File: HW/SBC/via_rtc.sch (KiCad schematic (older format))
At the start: 5 parts, among them J2 CONN_02X07, J3 CONN_02X07, U6 WD65C22, U7 DS1511Y+

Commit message: Updates to pcb and monitor.
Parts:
- J2, J3: footprint Pin_Headers:Pin_Header_Straight_2x07_Pitch2.54mm -> Connect:IDC_Header_Straight_14pins
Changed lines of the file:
@@
 F 0 "J2" H 1550 2825 50  0000 C CNN
 F 1 "CONN_02X07" V 1550 2425 50  0000 C CNN
-F 2 "Pin_Headers:Pin_Header_Straight_2x07_Pitch2.54mm" H 1550 1225 50  0001 C CNN
+F 2 "Connect:IDC_Header_Straight_14pins" H 1550 1225 50  0001 C CNN
 F 3 "" H 1550 1225 50  0001 C CNN
 	1    1550 2425
@@
 F 0 "J3" H 1550 4350 50  0000 C CNN
 F 1 "CONN_02X07" V 1550 3950 50  0000 C CNN
-F 2 "Pin_Headers:Pin_Header_Straight_2x07_Pitch2.54mm" H 1550 2750 50  0001 C CNN
+F 2 "Connect:IDC_Header_Straight_14pins" H 1550 2750 50  0001 C CNN
 F 3 "" H 1550 2750 50  0001 C CNN
 	1    1550 3950
@@
 $EndComp
 $Comp
-L VCC #PWR012
+L VCC #PWR013
 U 1 1 58D69383
 P 1125 4350
-F 0 "#PWR012" H 1125 4200 50  0001 C CNN
+F 0 "#PWR013" H 1125 4200 50  0001 C CNN
 F 1 "VCC" H 1125 4500 50  0000 C CNN
 F 2 "" H 1125 4350 50  0001 C CNN
@@
 $EndComp
 $Comp
-L GND #PWR013
+L GND #PWR014
 U 1 1 58D6939F
 P 1125 3450
-F 0 "#PWR013" H 1125 3200 50  0001 C CNN
+F 0 "#PWR014" H 1125 3200 50  0001 C CNN
 F 1 "GND" H 1125 3300 50  0000 C CNN
 F 2 "" H 1125 3450 50  0001 C CNN
@@
 $EndComp
 $Comp
-L GND #PWR014
+L GND #PWR015
 U 1 1 58D6973D
 P 1125 1950
-F 0 "#PWR014" H 1125 1700 50  0001 C CNN
+F 0 "#PWR015" H 1125 1700 50  0001 C CNN
 F 1 "GND" H 1125 1800 50  0000 C CNN
 F 2 "" H 1125 1950 50  0001 C CNN
@@
 $EndComp
 $Comp
-L VCC #PWR015
+L VCC #PWR016
 U 1 1 58D69759
 P 1125 2825
-F 0 "#PWR015" H 1125 2675 50  0001 C CNN
+F 0 "#PWR016" H 1125 2675 50  0001 C CNN
 F 1 "VCC" H 1125 2975 50  0000 C CNN
 F 2 "" H 1125 2825 50  0001 C CNN
@@
 $EndComp
 $Comp
-L VCC #PWR016
+L VCC #PWR017
 U 1 1 58D6982A
 P 4275 3550
-F 0 "#PWR016" H 4275 3400 50  0001 C CNN
+F 0 "#PWR017" H 4275 3400 50  0001 C CNN
 F 1 "VCC" H 4275 3700 50  0000 C CNN
 F 2 "" H 4275 3550 50  0001 C CNN
@@
 ~RES
 $Comp
-L GND #PWR017
+L GND #PWR018
 U 1 1 58D6B152
 P 7825 3725
-F 0 "#PWR017" H 7825 3475 50  0001 C CNN
+F 0 "#PWR018" H 7825 3475 50  0001 C CNN
 F 1 "GND" H 7825 3575 50  0000 C CNN
 F 2 "" H 7825 3725 50  0001 C CNN
@@
 $EndComp
 $Comp
-L VCC #PWR018
+L VCC #PWR019
 U 1 1 58D6B2C3
 P 7900 1850
-F 0 "#PWR018" H 7900 1700 50  0001 C CNN
+F 0 "#PWR019" H 7900 1700 50  0001 C CNN
 F 1 "VCC" H 7900 2000 50  0000 C CNN
 F 2 "" H 7900 1850 50  0001 C CNN
@@
 The intention is to use a WDC65C22\nso a diod has been added.
 $Comp
-L VCC #PWR019
+L VCC #PWR020
 U 1 1 58D8610D
 P 3400 1550
-F 0 "#PWR019" H 3400 1400 50  0001 C CNN
+F 0 "#PWR020" H 3400 1400 50  0001 C CNN
 F 1 "VCC" H 3400 1700 50  0000 C CNN
 F 2 "" H 3400 1550 50  0001 C CNN
@@
 	8450 2975 8775 2975
 $Comp
-L GND #PWR020
+L GND #PWR021
 U 1 1 58D875DB
 P 3400 4825
-F 0 "#PWR020" H 3400 4575 50  0001 C CNN
+F 0 "#PWR021" H 3400 4575 50  0001 C CNN
 F 1 "GND" H 3400 4675 50  0000 C CNN
 F 2 "" H 3400 4825 50  0001 C CNN

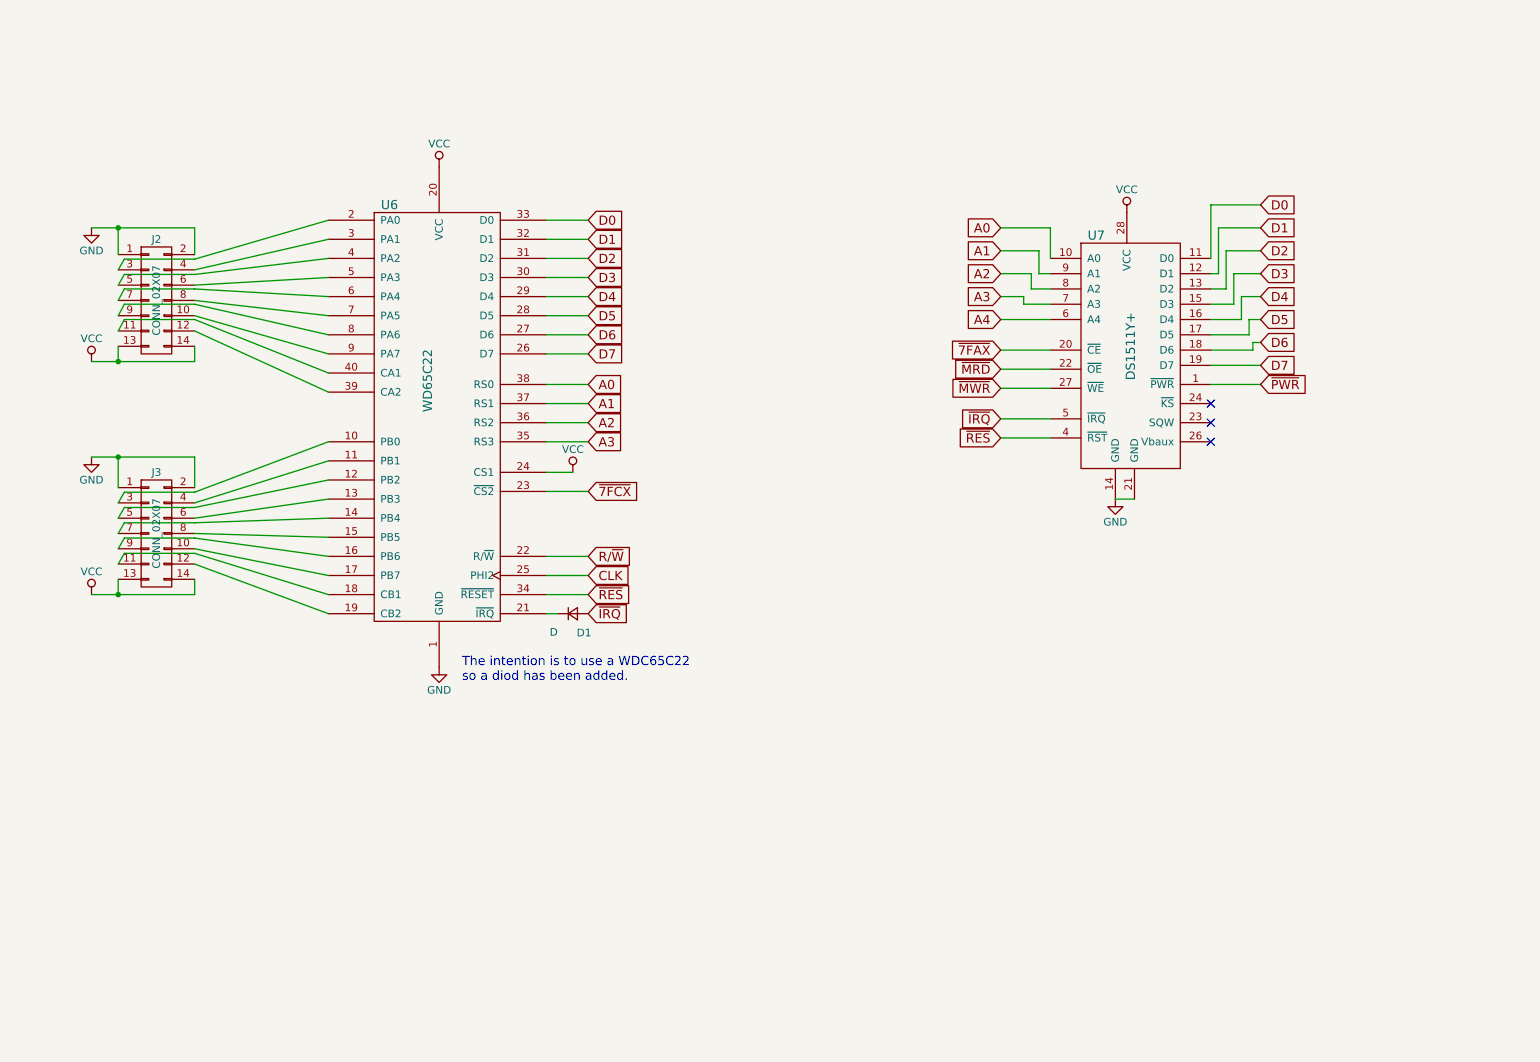
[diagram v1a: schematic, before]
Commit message: Schema changes to SBC
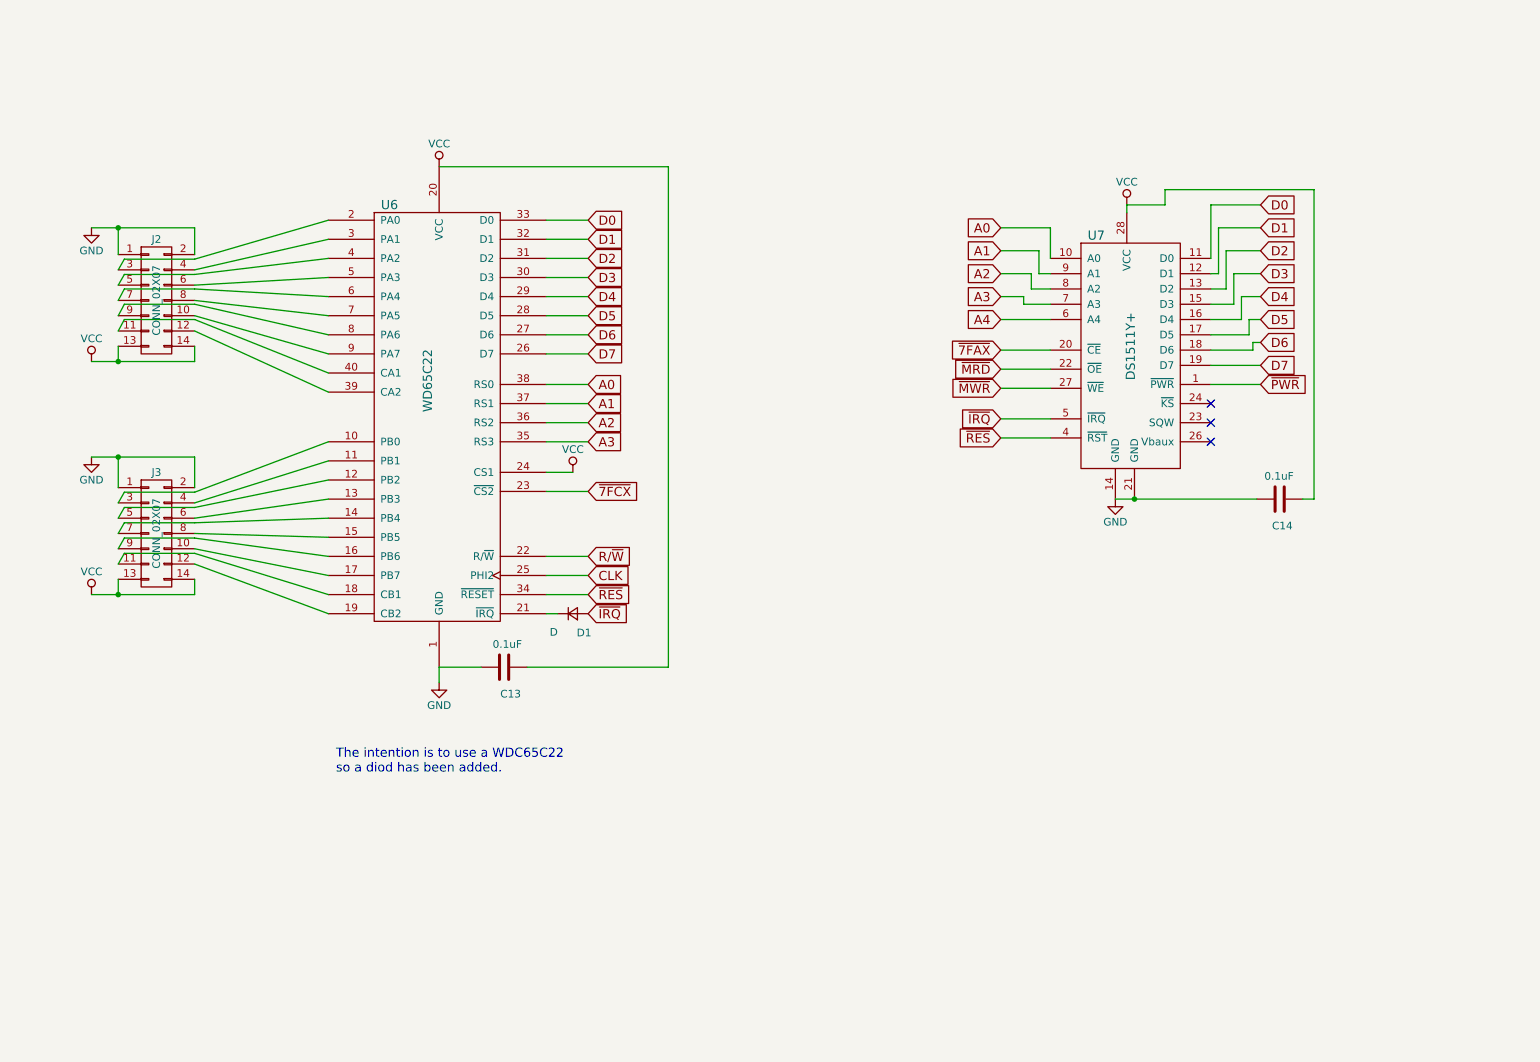
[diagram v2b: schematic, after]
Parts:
- added C13, C14: 0.1uF, Capacitors_ThroughHole:C_Disc_D3.8mm_W2.6mm_P2.50mm, symbol C
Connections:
- net GND: now also C13.2, C14.2
- net VCC: now also C13.1, C14.1
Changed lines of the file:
@@
 L VCC #PWR019
 U 1 1 58D6B2C3
-P 7900 1850
-F 0 "#PWR019" H 7900 1700 50  0001 C CNN
-F 1 "VCC" H 7900 2000 50  0000 C CNN
-F 2 "" H 7900 1850 50  0001 C CNN
-F 3 "" H 7900 1850 50  0001 C CNN
-	1    7900 1850
+P 7900 1800
+F 0 "#PWR019" H 7900 1650 50  0001 C CNN
+F 1 "VCC" H 7900 1950 50  0000 C CNN
+F 2 "" H 7900 1800 50  0001 C CNN
+F 3 "" H 7900 1800 50  0001 C CNN
+	1    7900 1800
 	1    0    0    -1
 $EndComp
@@
 Text GLabel 8775 2975 2    60   Input ~ 0
 ~PWR
-Text Notes 3550 4925 0    60   ~ 0
+Text Notes 2725 5525 0    60   ~ 0
 The intention is to use a WDC65C22\nso a diod has been added.
 $Comp
@@
 	1    0    0    -1
 $EndComp
+$Comp
+L GND #PWR021
+U 1 1 58D875DB
+P 3400 4925
+F 0 "#PWR021" H 3400 4675 50  0001 C CNN
+F 1 "GND" H 3400 4775 50  0000 C CNN
+F 2 "" H 3400 4925 50  0001 C CNN
+F 3 "" H 3400 4925 50  0001 C CNN
+	1    3400 4925
+	1    0    0    -1
+$EndComp
+$Comp
+L C C13
+U 1 1 5907389E
+P 3825 4825
+F 0 "C13" V 4000 4800 50  0000 L CNN
+F 1 "0.1uF" V 3675 4750 50  0000 L CNN
+F 2 "Capacitors_ThroughHole:C_Disc_D3.8mm_W2.6mm_P2.50mm" H 3863 4675 50  0001 C CNN
+F 3 "" H 3825 4825 50  0001 C CNN
+	1    3825 4825
+	0    1    1    0
+$EndComp
 Wire Wire Line
 	7400 2550 7075 2550
@@
 	8450 1800 8775 1800
 Wire Wire Line
-	7950 3725 7825 3725
+	7825 3725 8750 3725
 Wire Wire Line
 	8450 2975 8775 2975
+Wire Wire Line
+	3400 4825 3400 4925
+Wire Wire Line
+	3675 4825 3400 4825
+Wire Wire Line
+	3975 4825 4900 4825
+Wire Wire Line
+	4900 4825 4900 1550
+Wire Wire Line
+	4900 1550 3400 1550
 $Comp
-L GND #PWR021
-U 1 1 58D875DB
-P 3400 4825
-F 0 "#PWR021" H 3400 4575 50  0001 C CNN
-F 1 "GND" H 3400 4675 50  0000 C CNN
-F 2 "" H 3400 4825 50  0001 C CNN
-F 3 "" H 3400 4825 50  0001 C CNN
-	1    3400 4825
-	1    0    0    -1
-$EndComp
+L C C14
+U 1 1 59074B76
+P 8900 3725
+F 0 "C14" V 9075 3675 50  0000 L CNN
+F 1 "0.1uF" V 8750 3625 50  0000 L CNN
+F 2 "Capacitors_ThroughHole:C_Disc_D3.8mm_W2.6mm_P2.50mm" H 8938 3575 50  0001 C CNN
+F 3 "" H 8900 3725 50  0001 C CNN
+	1    8900 3725
+	0    1    1    0
+$EndComp
+Connection ~ 7950 3725
+Wire Wire Line
+	7900 1850 7900 1800
+Wire Wire Line
+	9050 3725 9125 3725
+Wire Wire Line
+	9125 3725 9125 1700
+Wire Wire Line
+	9125 1700 8150 1700
+Wire Wire Line
+	8150 1700 8150 1800
+Wire Wire Line
+	8150 1800 7900 1800
 $EndSCHEMATC

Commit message: New board layout. WIP
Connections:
- net GND: no longer C13.2, C14.2, U6.1 (GND), U7.14 (GND), U7.21 (GND)
- net VCC: no longer C13.1, C14.1, U6.20 (VCC), U7.28 (VCC)
- new net: C13.2, U6.1 (GND)
- new net: C13.1, U6.20 (VCC)
- new net: C14.2, U7.14 (GND), U7.21 (GND)
- new net: C14.1, U7.28 (VCC)
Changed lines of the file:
@@
 Text GLabel 7075 3325 0    60   Input ~ 0
 ~RES
-$Comp
-L GND #PWR018
-U 1 1 58D6B152
-P 7825 3725
-F 0 "#PWR018" H 7825 3475 50  0001 C CNN
-F 1 "GND" H 7825 3575 50  0000 C CNN
-F 2 "" H 7825 3725 50  0001 C CNN
-F 3 "" H 7825 3725 50  0001 C CNN
-	1    7825 3725
-	1    0    0    -1
-$EndComp
-$Comp
-L VCC #PWR019
-U 1 1 58D6B2C3
-P 7900 1800
-F 0 "#PWR019" H 7900 1650 50  0001 C CNN
-F 1 "VCC" H 7900 1950 50  0000 C CNN
-F 2 "" H 7900 1800 50  0001 C CNN
-F 3 "" H 7900 1800 50  0001 C CNN
-	1    7900 1800
-	1    0    0    -1
-$EndComp
 NoConn ~ 8450 3100
 NoConn ~ 8450 3225
@@
 Text Notes 2725 5525 0    60   ~ 0
 The intention is to use a WDC65C22\nso a diod has been added.
-$Comp
-L VCC #PWR020
-U 1 1 58D8610D
-P 3400 1550
-F 0 "#PWR020" H 3400 1400 50  0001 C CNN
-F 1 "VCC" H 3400 1700 50  0000 C CNN
-F 2 "" H 3400 1550 50  0001 C CNN
-F 3 "" H 3400 1550 50  0001 C CNN
-	1    3400 1550
-	1    0    0    -1
-$EndComp
-$Comp
-L GND #PWR021
-U 1 1 58D875DB
-P 3400 4925
-F 0 "#PWR021" H 3400 4675 50  0001 C CNN
-F 1 "GND" H 3400 4775 50  0000 C CNN
-F 2 "" H 3400 4925 50  0001 C CNN
-F 3 "" H 3400 4925 50  0001 C CNN
-	1    3400 4925
-	1    0    0    -1
-$EndComp
 $Comp
 L C C13
@@
 	8450 2975 8775 2975
 Wire Wire Line
-	3400 4825 3400 4925
-Wire Wire Line
 	3675 4825 3400 4825
 Wire Wire Line
@@
 Wire Wire Line
 	4900 4825 4900 1550
-Wire Wire Line
-	4900 1550 3400 1550
 $Comp
 L C C14
@@
 Wire Wire Line
 	8150 1800 7900 1800
+Wire Wire Line
+	4900 1550 3400 1550
 $EndSCHEMATC

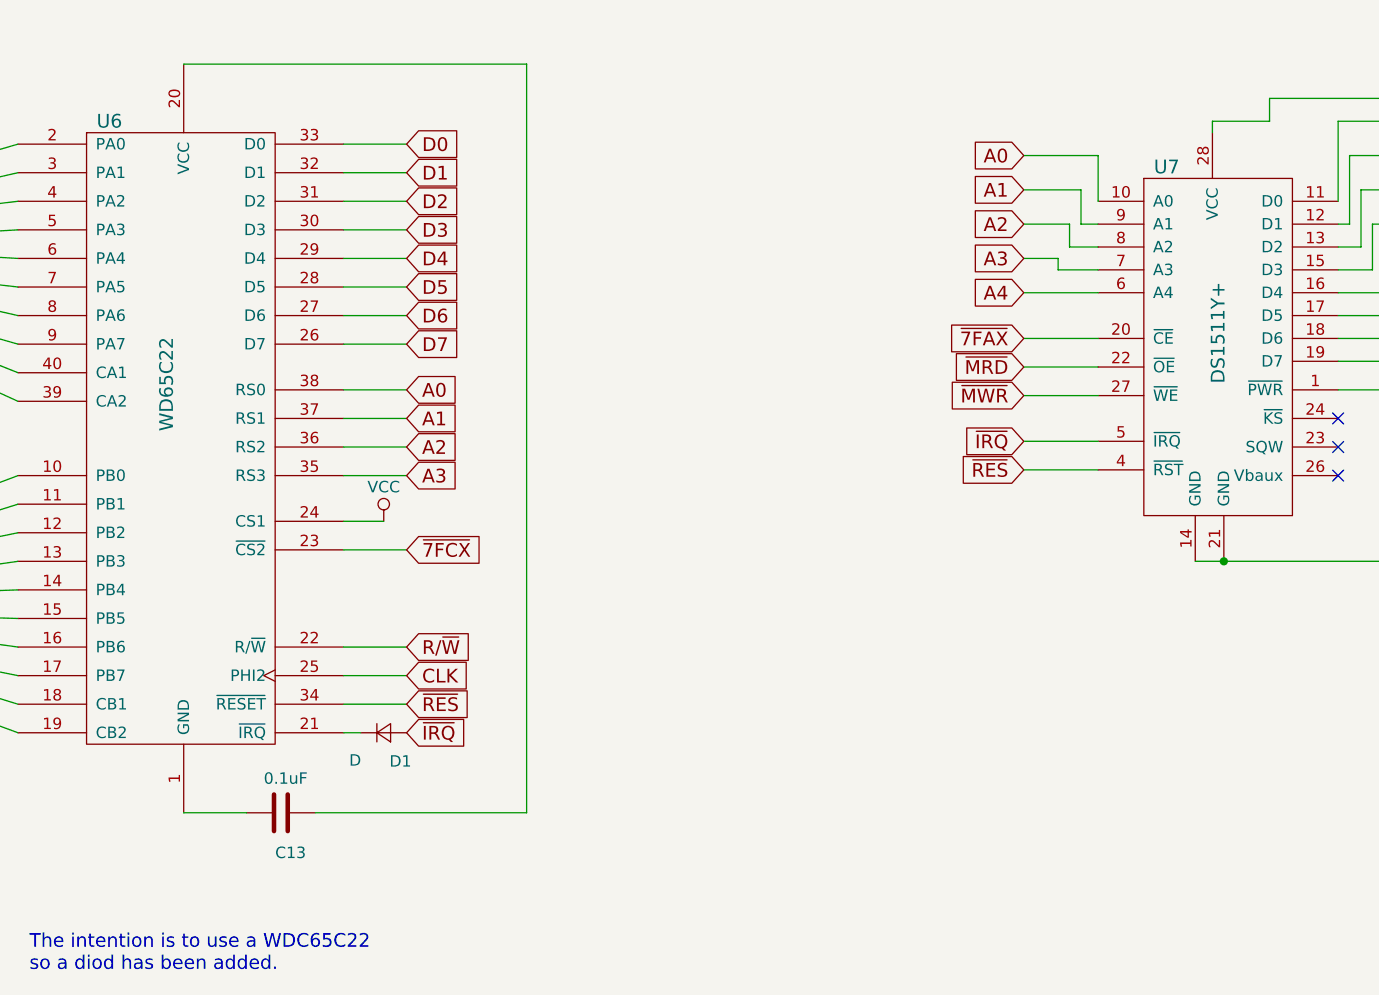
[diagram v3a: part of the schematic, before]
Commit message: New SBC PCB. Started to split pluto_kernel.asm into bios, monitor and miniassembler/disassembler. Various other updates.
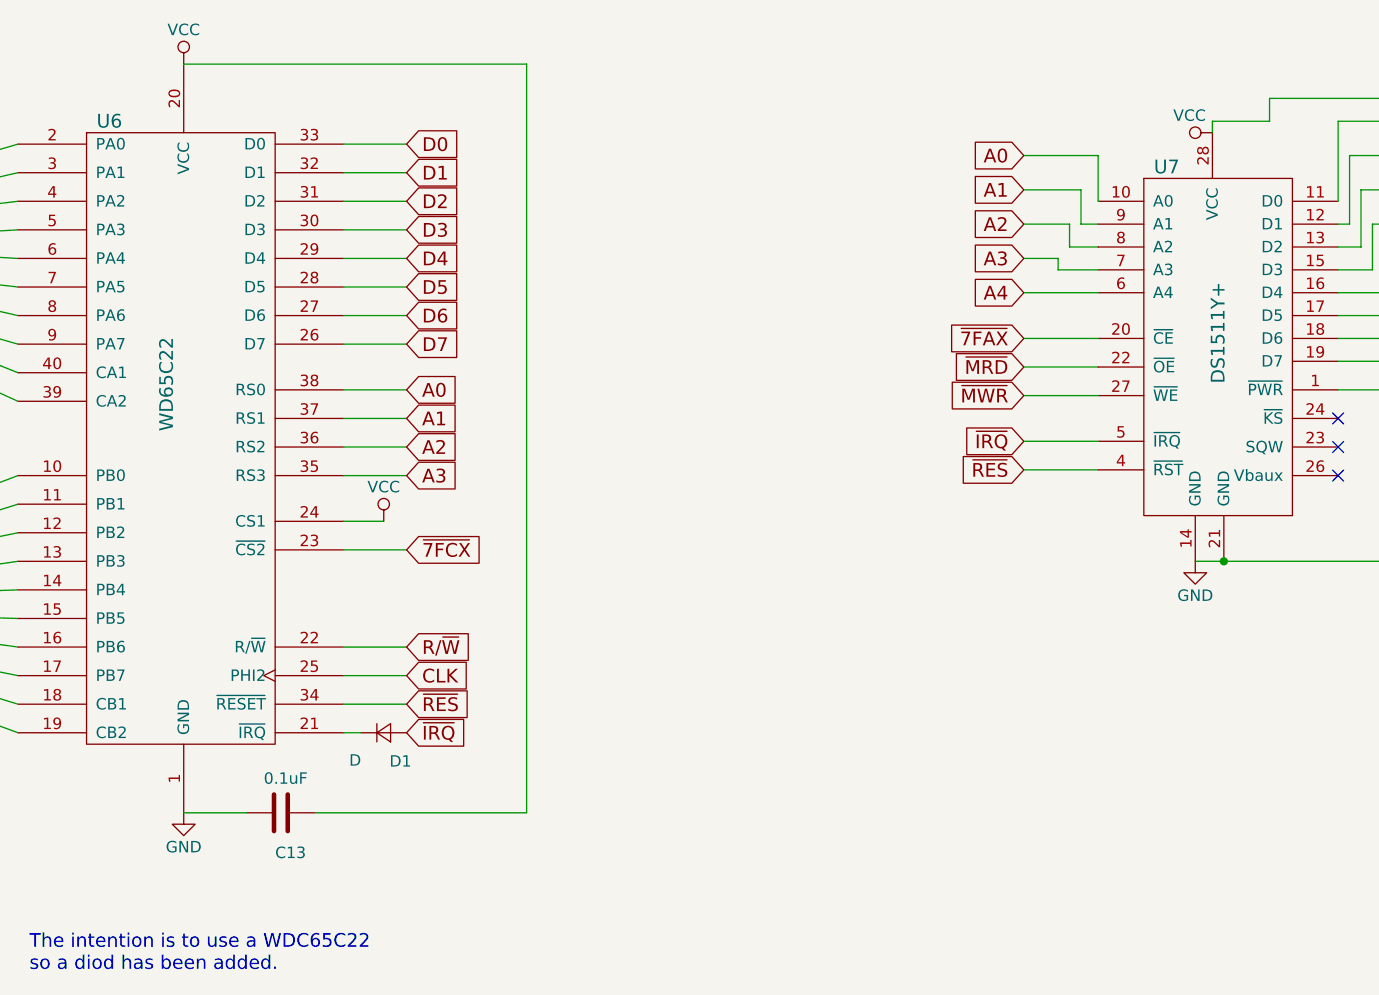
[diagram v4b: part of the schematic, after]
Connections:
- net GND: now also C13.2, C14.2, U6.1 (GND), U7.14 (GND), U7.21 (GND)
- net VCC: now also C13.1, C14.1, U6.20 (VCC), U7.28 (VCC)
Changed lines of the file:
@@
 $EndComp
 $Comp
-L VCC #PWR013
+L VCC #PWR010
 U 1 1 58D69383
 P 1125 4350
-F 0 "#PWR013" H 1125 4200 50  0001 C CNN
+F 0 "#PWR010" H 1125 4200 50  0001 C CNN
 F 1 "VCC" H 1125 4500 50  0000 C CNN
 F 2 "" H 1125 4350 50  0001 C CNN
@@
 $EndComp
 $Comp
-L GND #PWR014
+L GND #PWR011
 U 1 1 58D6939F
 P 1125 3450
-F 0 "#PWR014" H 1125 3200 50  0001 C CNN
+F 0 "#PWR011" H 1125 3200 50  0001 C CNN
 F 1 "GND" H 1125 3300 50  0000 C CNN
 F 2 "" H 1125 3450 50  0001 C CNN
@@
 $EndComp
 $Comp
-L GND #PWR015
+L GND #PWR012
 U 1 1 58D6973D
 P 1125 1950
-F 0 "#PWR015" H 1125 1700 50  0001 C CNN
+F 0 "#PWR012" H 1125 1700 50  0001 C CNN
 F 1 "GND" H 1125 1800 50  0000 C CNN
 F 2 "" H 1125 1950 50  0001 C CNN
@@
 $EndComp
 $Comp
-L VCC #PWR016
+L VCC #PWR013
 U 1 1 58D69759
 P 1125 2825
-F 0 "#PWR016" H 1125 2675 50  0001 C CNN
+F 0 "#PWR013" H 1125 2675 50  0001 C CNN
 F 1 "VCC" H 1125 2975 50  0000 C CNN
 F 2 "" H 1125 2825 50  0001 C CNN
@@
 $EndComp
 $Comp
-L VCC #PWR017
+L VCC #PWR014
 U 1 1 58D6982A
 P 4275 3550
-F 0 "#PWR017" H 4275 3400 50  0001 C CNN
+F 0 "#PWR014" H 4275 3400 50  0001 C CNN
 F 1 "VCC" H 4275 3700 50  0000 C CNN
 F 2 "" H 4275 3550 50  0001 C CNN
@@
 Wire Wire Line
 	4900 1550 3400 1550
+$Comp
+L VCC #PWR015
+U 1 1 5924C298
+P 3400 1550
+F 0 "#PWR015" H 3400 1400 50  0001 C CNN
+F 1 "VCC" H 3400 1700 50  0000 C CNN
+F 2 "" H 3400 1550 50  0001 C CNN
+F 3 "" H 3400 1550 50  0001 C CNN
+	1    3400 1550
+	1    0    0    -1
+$EndComp
+$Comp
+L GND #PWR016
+U 1 1 5924C3BB
+P 3400 4825
+F 0 "#PWR016" H 3400 4575 50  0001 C CNN
+F 1 "GND" H 3400 4675 50  0000 C CNN
+F 2 "" H 3400 4825 50  0001 C CNN
+F 3 "" H 3400 4825 50  0001 C CNN
+	1    3400 4825
+	1    0    0    -1
+$EndComp
+$Comp
+L VCC #PWR?
+U 1 1 5924C55A
+P 7900 1850
+F 0 "#PWR?" H 7900 1700 50  0001 C CNN
+F 1 "VCC" V 7975 1950 50  0000 C CNN
+F 2 "" H 7900 1850 50  0001 C CNN
+F 3 "" H 7900 1850 50  0001 C CNN
+	1    7900 1850
+	0    -1   -1   0
+$EndComp
+$Comp
+L GND #PWR?
+U 1 1 5924C775
+P 7825 3725
+F 0 "#PWR?" H 7825 3475 50  0001 C CNN
+F 1 "GND" H 7825 3575 50  0000 C CNN
+F 2 "" H 7825 3725 50  0001 C CNN
+F 3 "" H 7825 3725 50  0001 C CNN
+	1    7825 3725
+	1    0    0    -1
+$EndComp
 $EndSCHEMATC
